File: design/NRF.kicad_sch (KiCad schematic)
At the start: 18 parts, among them J2 Conn_Coaxial, U4 nRF24L01P, X2 16MHz

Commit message: Agregue LCSC Part #
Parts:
- L3: LCSC (none) -> C6364698; MPN LQW18AS8N2G00D -> (none); Manufacturer Murata Electronics -> APV
- L4: LCSC (none) -> C13818; MPN LCCI0603S3N9GTAR -> (none); Manufacturer KYOCERA AVX -> Sunlord
- L5: LCSC (none) -> C162551; MPN BSCH001608082N7S00 -> LQG18HN2N7S00D; Manufacturer Pulse Electronics -> Murata
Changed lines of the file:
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@@
 			)
 		)
-		(property "Manufacturer" "Murata Electronics"
+		(property "Manufacturer" "APV"
 			(at 182.88 80.01 0)
 			(effects
@@
 			)
 		)
-		(property "MPN" "LQW18AS8N2G00D"
+		(property "MPN" ""
+			(at 182.88 80.01 0)
+			(effects
+				(font
+					(size 1.27 1.27)
+				)
+				(hide yes)
+			)
+		)
+		(property "LCSC" "C6364698"
 			(at 182.88 80.01 0)
 			(effects
@@
 			)
 		)
-		(property "Manufacturer" " KYOCERA AVX"
-			(at 195.58 73.66 0)
-			(effects
-				(font
-					(size 1.27 1.27)
-				)
-				(hide yes)
-			)
-		)
-		(property "MPN" "LCCI0603S3N9GTAR"
+		(property "Manufacturer" " Sunlord"
+			(at 195.58 73.66 0)
+			(effects
+				(font
+					(size 1.27 1.27)
+				)
+				(hide yes)
+			)
+		)
+		(property "MPN" ""
+			(at 195.58 73.66 0)
+			(effects
+				(font
+					(size 1.27 1.27)
+				)
+				(hide yes)
+			)
+		)
+		(property "LCSC" "C13818"
 			(at 195.58 73.66 0)
 			(effects
@@
 			)
 		)
-		(property "Manufacturer" " Pulse Electronics"
-			(at 196.85 86.36 0)
-			(effects
-				(font
-					(size 1.27 1.27)
-				)
-				(hide yes)
-			)
-		)
-		(property "MPN" "BSCH001608082N7S00"
-			(at 196.85 86.36 0)
-			(effects
+		(property "Manufacturer" "Murata"
+			(at 196.85 86.36 0)
+			(effects
+				(font
+					(size 1.27 1.27)
+				)
+				(hide yes)
+			)
+		)
+		(property "MPN" "LQG18HN2N7S00D"
+			(at 196.85 86.36 0)
+			(effects
+				(font
+					(size 1.27 1.27)
+				)
+				(hide yes)
+			)
+		)
+		(property "LCSC" "C162551"
+			(at 196.85 86.36 0)
+			(effects

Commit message: Agregue LCSC Part # a algunas resistencias
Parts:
- R16: LCSC (none) -> C115416
- R17: MPN RC0603JR-0722KL -> (none)
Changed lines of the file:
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@@
+			)
+		)
+		(property "LCSC" "C115416"
+			(at 154.94 54.61 0)
+			(effects
+				(font
+					(size 1.27 1.27)
+				)
+				(hide yes)
 			)
 		)
@@
 			)
 		)
-		(property "MPN" "RC0603JR-0722KL"
+		(property "MPN" ""
 			(at 171.45 116.84 0)
 			(effects

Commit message: Correccion de algunos DRC
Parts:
- R17: LCSC (none) -> C105578; MPN (none) -> RC0603FR-071ML
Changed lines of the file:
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@@
 			)
 		)
-		(property "MPN" ""
+		(property "MPN" "RC0603FR-071ML"
 			(at 171.45 116.84 0)
 			(effects
+				(font
+					(size 1.27 1.27)
+				)
+				(hide yes)
+			)
+		)
+		(property "LCSC" "C105578"
+			(at 171.45 116.84 0)
+			(effects

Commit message: Correccion de DRC
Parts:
- U4: LCSC (none) -> C8791
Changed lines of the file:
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@@
+			)
+		)
+		(property "LCSC" "C8791"
+			(at 146.05 81.28 0)
+			(effects
+				(font
+					(size 1.27 1.27)
+				)
+				(hide yes)
 			)
 		)

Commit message: Agrego # de los cristales
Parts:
- J2: footprint Connector_Coaxial:SMA_Amphenol_901-143_Horizontal -> Connector_Coaxial:SMA_Amphenol_901-144_Vertical
- X2: LCSC (none) -> C12676; MPN ECS-160-20-3X-TR -> X49SM16MSD2SC; Manufacturer ECS Inc. -> YXC Crystal Oscillators
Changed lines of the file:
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@@
 			)
 		)
-		(property "Manufacturer" "ECS Inc."
+		(property "Manufacturer" "YXC Crystal Oscillators"
 			(at 157.48 116.84 0)
 			(effects
@@
 			)
 		)
-		(property "MPN" "ECS-160-20-3X-TR"
+		(property "MPN" "X49SM16MSD2SC"
+			(at 157.48 116.84 0)
+			(effects
+				(font
+					(size 1.27 1.27)
+				)
+				(hide yes)
+			)
+		)
+		(property "LCSC" "C12676"
 			(at 157.48 116.84 0)
 			(effects
@@
 			)
 		)
-		(property "Footprint" "Connector_Coaxial:SMA_Amphenol_901-143_Horizontal"
+		(property "Footprint" "Connector_Coaxial:SMA_Amphenol_901-144_Vertical"
 			(at 238.76 73.66 0)
 			(effects

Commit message: Abaratando costos
Cambios en numeros de jlcpcb, pasados a componentes básicos
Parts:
- C31, C32, C33, C34, C35, C36, C37, C38, C39, C40, J2, L3, L4, L5, U4, X2: now left out of the parts list
- R16: LCSC C115416 -> C31850; now left out of the parts list
- R17: LCSC C105578 -> C22935; now left out of the parts list
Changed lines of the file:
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@@
 		(unit 1)
 		(exclude_from_sim no)
-		(in_bom yes)
+		(in_bom no)
 		(on_board yes)
 		(dnp no)
@@
 		(unit 1)
 		(exclude_from_sim no)
-		(in_bom yes)
+		(in_bom no)
 		(on_board yes)
 		(dnp no)
@@
 		(unit 1)
 		(exclude_from_sim no)
-		(in_bom yes)
+		(in_bom no)
 		(on_board yes)
 		(dnp no)
@@
 		(unit 1)
 		(exclude_from_sim no)
-		(in_bom yes)
+		(in_bom no)
 		(on_board yes)
 		(dnp no)
@@
 		(unit 1)
 		(exclude_from_sim no)
-		(in_bom yes)
+		(in_bom no)
 		(on_board yes)
 		(dnp no)
@@
 		(unit 1)
 		(exclude_from_sim no)
-		(in_bom yes)
+		(in_bom no)
 		(on_board yes)
 		(dnp no)
@@
 		(unit 1)
 		(exclude_from_sim no)
-		(in_bom yes)
+		(in_bom no)
 		(on_board yes)
 		(dnp no)
@@
 		(unit 1)
 		(exclude_from_sim no)
-		(in_bom yes)
+		(in_bom no)
 		(on_board yes)
 		(dnp no)
@@
 		(unit 1)
 		(exclude_from_sim no)
-		(in_bom yes)
+		(in_bom no)
 		(on_board yes)
 		(dnp no)
@@
 		(unit 1)
 		(exclude_from_sim no)
-		(in_bom yes)
+		(in_bom no)
 		(on_board yes)
 		(dnp no)
@@
 		(unit 1)
 		(exclude_from_sim no)
-		(in_bom yes)
+		(in_bom no)
 		(on_board yes)
 		(dnp no)
@@
 		(unit 1)
 		(exclude_from_sim no)
-		(in_bom yes)
+		(in_bom no)
 		(on_board yes)
 		(dnp no)
@@
 		(unit 1)
 		(exclude_from_sim no)
-		(in_bom yes)
+		(in_bom no)
 		(on_board yes)
 		(dnp no)
@@
 		(unit 1)
 		(exclude_from_sim no)
-		(in_bom yes)
+		(in_bom no)
 		(on_board yes)
 		(dnp no)
@@
 			)
 		)
-		(property "LCSC" "C115416"
+		(property "LCSC" "C31850"
 			(at 154.94 54.61 0)
 			(effects
@@
 		(unit 1)
 		(exclude_from_sim no)
-		(in_bom yes)
+		(in_bom no)
 		(on_board yes)
 		(dnp no)
@@
 		(unit 1)
 		(exclude_from_sim no)
-		(in_bom yes)
+		(in_bom no)
 		(on_board yes)
 		(dnp no)
@@
 			)
 		)
-		(property "LCSC" "C105578"
+		(property "LCSC" "C22935"
 			(at 171.45 116.84 0)
 			(effects
@@
 		(unit 1)
 		(exclude_from_sim no)
-		(in_bom yes)
+		(in_bom no)
 		(on_board yes)
 		(dnp no)
@@
 		(unit 1)
 		(exclude_from_sim no)
-		(in_bom yes)
-		(on_board yes)
-		(dnp no)
+		(in_bom no)
+		(on_board yes)
+		(dnp no)

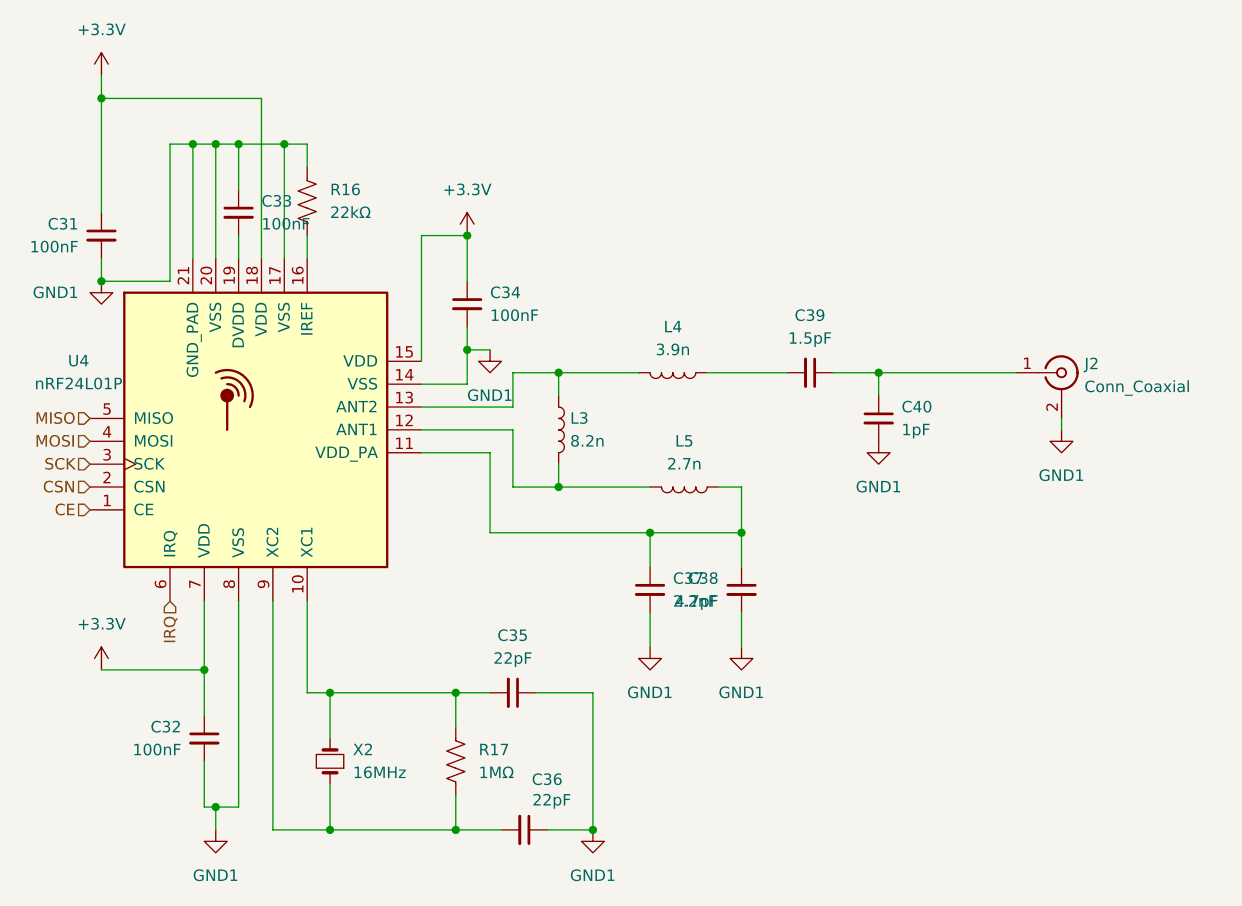
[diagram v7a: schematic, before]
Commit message: Sacado de NRF
Sacado de NRF, re-hecho constraints
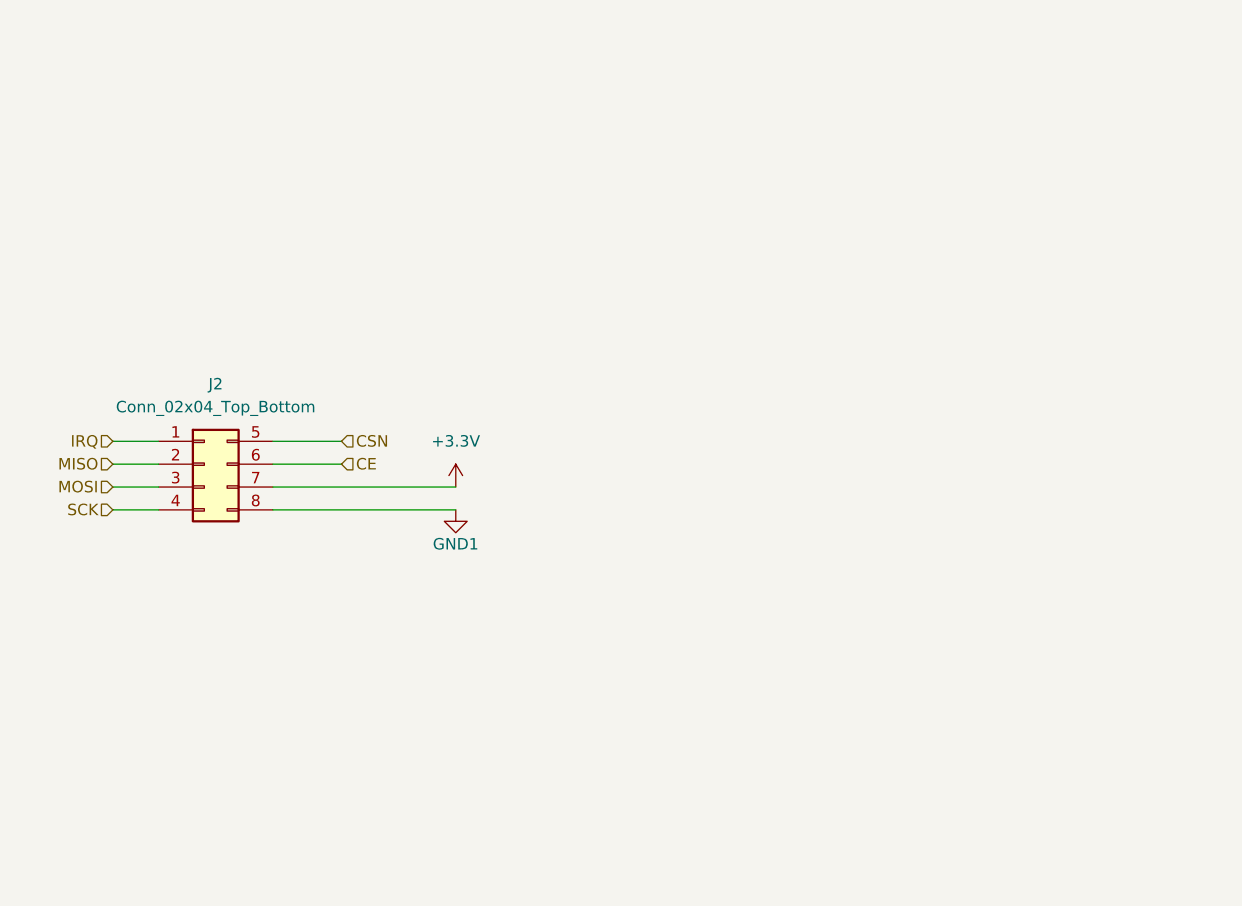
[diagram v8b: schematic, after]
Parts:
- removed C31, C32, C33, C34: 100nF, Capacitor_SMD:C_0603_1608Metric, symbol Device:C_Small
- removed C35, C36: 22pF, Capacitor_SMD:C_0603_1608Metric, symbol Device:C_Small
- removed C37: 2.2nF, Capacitor_SMD:C_0603_1608Metric, symbol Device:C_Small
- removed C38: 4.7pF, Capacitor_SMD:C_0603_1608Metric, symbol Device:C_Small
- removed C39: 1.5pF, Capacitor_SMD:C_0603_1608Metric, symbol Device:C_Small
- removed C40: 1pF, Capacitor_SMD:C_0603_1608Metric, symbol Device:C_Small
- removed J2: Conn_Coaxial, Connector_Coaxial:SMA_Amphenol_901-144_Vertical, symbol Connector:Conn_Coaxial
- removed L3: 8.2n, Inductor_SMD:L_0603_1608Metric_Pad1.05x0.95mm_HandSolder, symbol Device:L
- removed L4: 3.9n, Inductor_SMD:L_0603_1608Metric_Pad1.05x0.95mm_HandSolder, symbol Device:L
- removed L5: 2.7n, Inductor_SMD:L_0603_1608Metric_Pad1.05x0.95mm_HandSolder, symbol Device:L
- removed R16: 22kΩ, Resistor_SMD:R_0603_1608Metric, symbol Device:R_US
- removed R17: 1MΩ, Resistor_SMD:R_0603_1608Metric, symbol Device:R_US
- removed U4: nRF24L01P, Package_DFN_QFN:QFN-20-1EP_4x4mm_P0.5mm_EP2.5x2.5mm, symbol crf_2:nRF24L01P
- removed X2: 16MHz, Crystal:Crystal_SMD_HC49-SD, symbol Device:Crystal_Small
- added J2: Conn_02x04_Top_Bottom, Connector_PinHeader_2.54mm:PinHeader_2x04_P2.54mm_Vertical, symbol Connector_Generic:Conn_02x04_Top_Bottom
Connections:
- net +3.3V: now also J2.7 (Pin_7)
- net CE: now also J2.6 (Pin_6)
- net CSN: now also J2.5 (Pin_5)
- net GND1: now also J2.8 (Pin_8)
- net IRQ: now also J2.1 (Pin_1)
- net MISO: now also J2.2 (Pin_2)
- net MOSI: now also J2.3 (Pin_3)
- net SCK: now also J2.4 (Pin_4)
